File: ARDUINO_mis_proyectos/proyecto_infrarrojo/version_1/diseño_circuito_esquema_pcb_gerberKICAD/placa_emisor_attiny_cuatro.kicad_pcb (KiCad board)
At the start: 2 copper layers, 30.5 x 85.1 mm, 7 parts, among them J1 KY005, SW1 SW_Push, U1 ATtiny85V-10SU

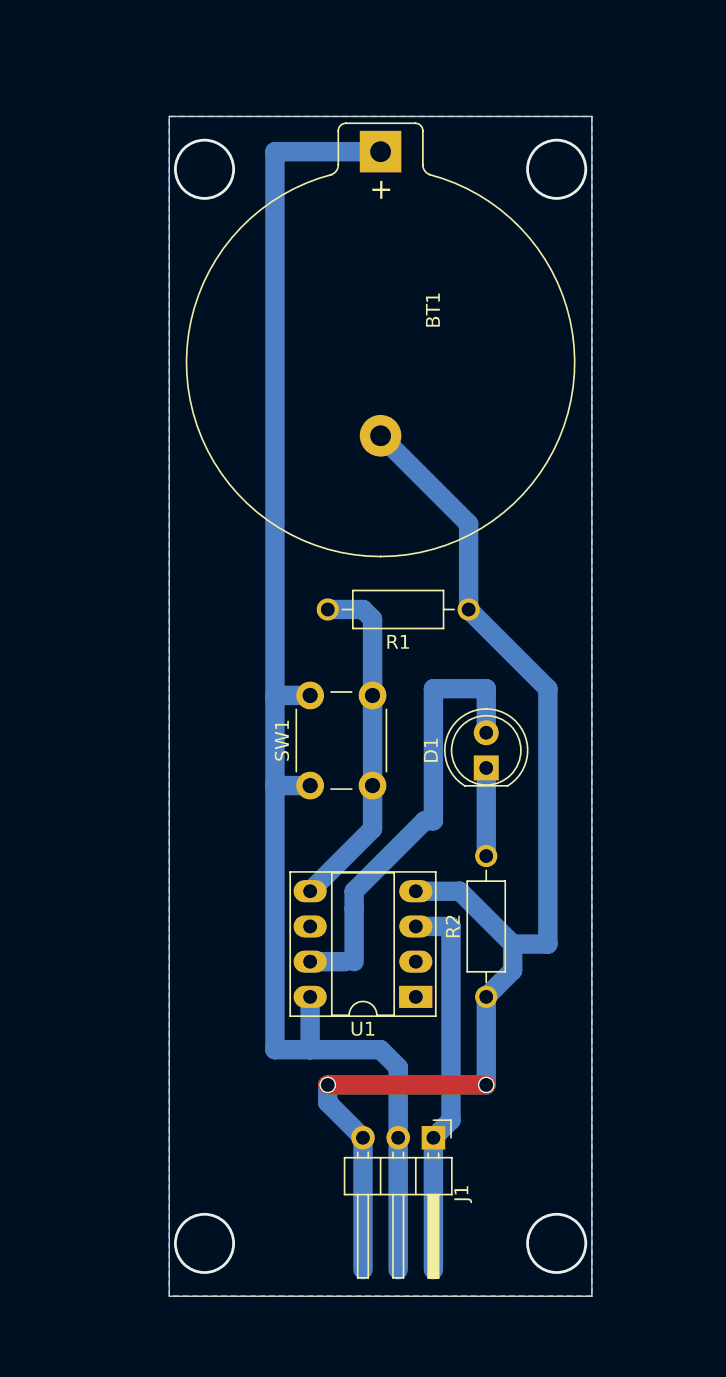
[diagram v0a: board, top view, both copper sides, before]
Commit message: Actualizando attiny IR Remote
Algunos cambios en los programas del attiny
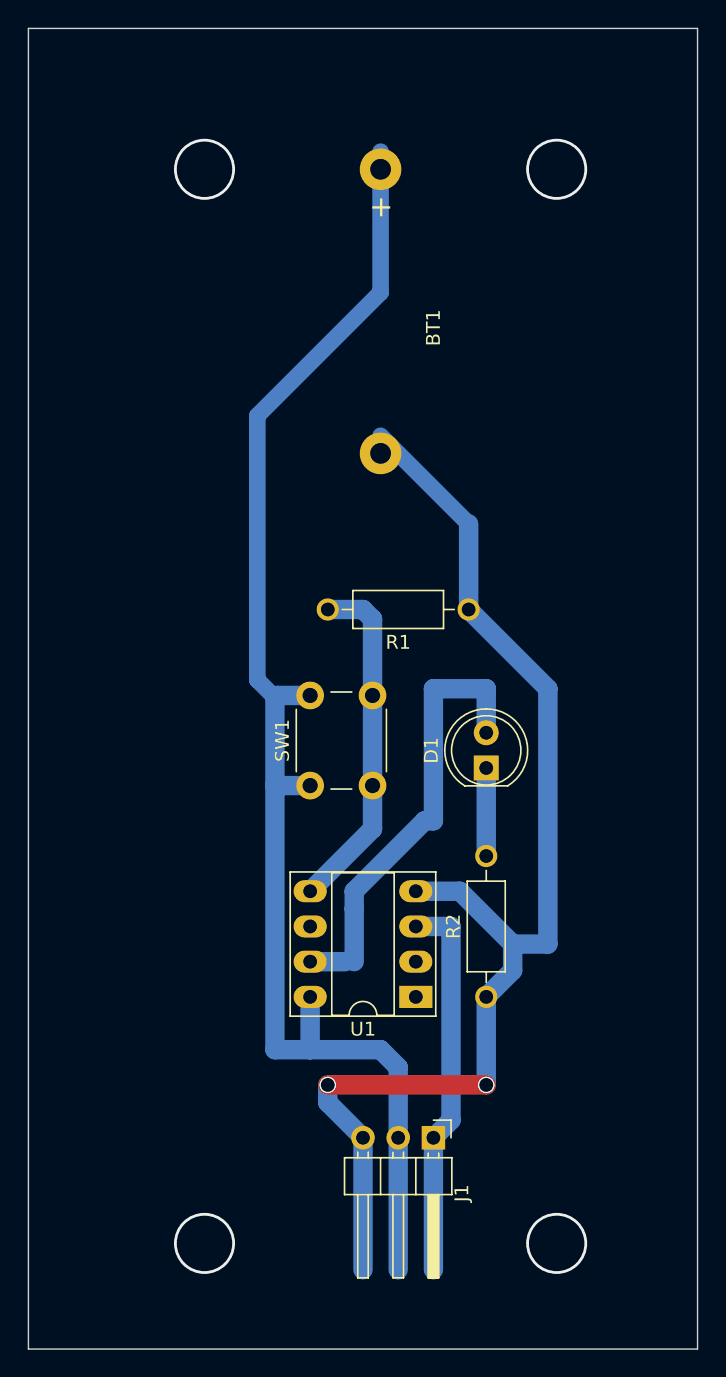
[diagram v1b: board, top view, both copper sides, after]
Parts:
- BT1: footprint Battery:BatteryHolder_Keystone_106_1x20mm -> modificados:BatteryHolder_mia_106_1x20
- moved BT1 1.27 mm to (142.2, 76.2)
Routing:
- net VCC: track 104.7 -> 101.3 mm
- removed copper zone on B.Cu, net GND
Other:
- board size 30.5 x 85.1 mm -> 48.3 x 95.2 mm
